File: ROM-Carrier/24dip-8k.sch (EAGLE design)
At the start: 7 parts

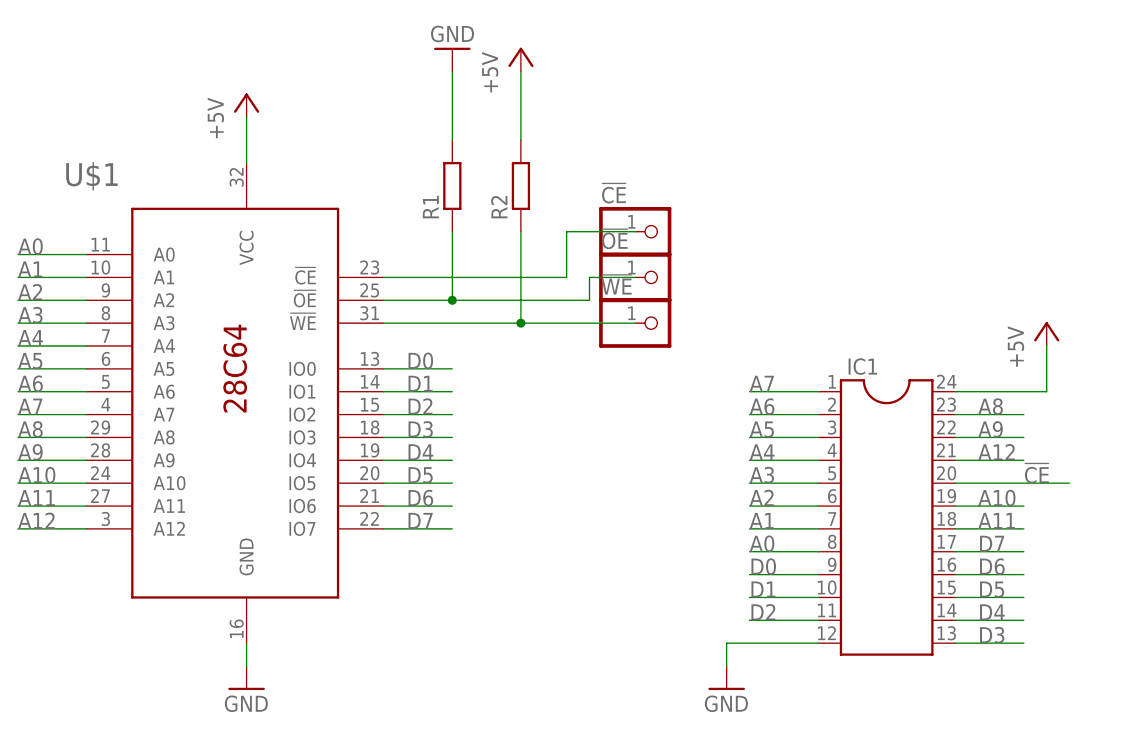
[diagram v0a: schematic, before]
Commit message: fix carrier board (was 24-9, needed to be 24-6) removed unnecessary z80 support from 8080 sim
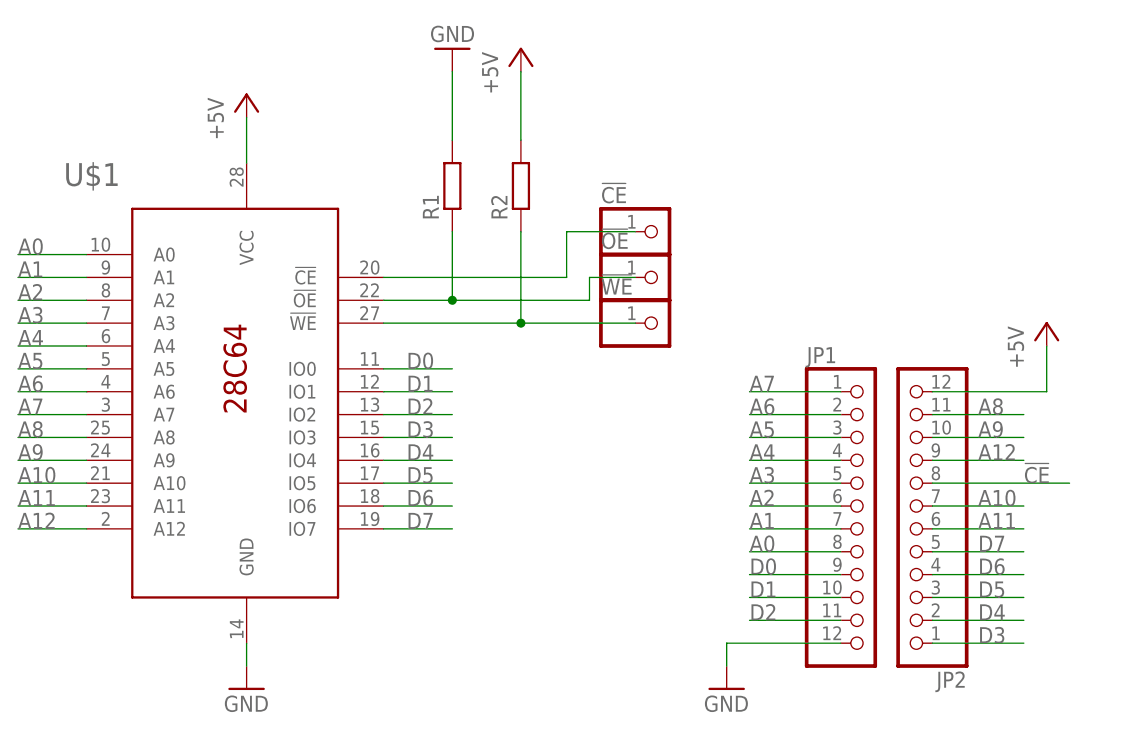
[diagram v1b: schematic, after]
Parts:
- removed IC1: (no value), ic-package:DIL24-9
- added JP1, JP2: (no value), pinhead:PINHD-1X12
- U$1: value AT28C64B32J -> AT28C64B28S; device eeprom:AT28C64B32J -> eeprom:AT28C64B28S
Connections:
- net !CE: now also JP2.8; no longer IC1.20
- net +5V: now also JP2.12; no longer IC1.24
- net A0: now also JP1.8; no longer IC1.8
- net A1: now also JP1.7; no longer IC1.7
- net A10: now also JP2.7; no longer IC1.19
- net A11: now also JP2.6; no longer IC1.18
- net A12: now also JP2.9; no longer IC1.21
- net A2: now also JP1.6; no longer IC1.6
- net A3: now also JP1.5; no longer IC1.5
- net A4: now also JP1.4; no longer IC1.4
- net A5: now also JP1.3; no longer IC1.3
- net A6: now also JP1.2; no longer IC1.2
- net A7: now also JP1.1; no longer IC1.1
- net A8: now also JP2.11; no longer IC1.23
- net A9: now also JP2.10; no longer IC1.22
- net D0: now also JP1.9; no longer IC1.9
- net D1: now also JP1.10; no longer IC1.10
- net D2: now also JP1.11; no longer IC1.11
- net D3: now also JP2.1; no longer IC1.13
- net D4: now also JP2.2; no longer IC1.14
- net D5: now also JP2.3; no longer IC1.15
- net D6: now also JP2.4; no longer IC1.16
- net D7: now also JP2.5; no longer IC1.17
- net GND: now also JP1.12; no longer IC1.12
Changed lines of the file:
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@@
 </classes>
 <parts>
-<part name="U$1" library="eeprom" deviceset="AT28C64B" device="32J"/>
-<part name="IC1" library="ic-package" deviceset="DIL24" device="-9"/>
+<part name="U$1" library="eeprom" deviceset="AT28C64B" device="28S" value="AT28C64B28S"/>
 <part name="R1" library="rcl" deviceset="R-EU_" device="R1206"/>
 <part name="R2" library="rcl" deviceset="R-EU_" device="R1206"/>
@@
 <part name="!OE" library="pinhead" deviceset="PINHD-1X1" device=""/>
 <part name="!WE" library="pinhead" deviceset="PINHD-1X1" device=""/>
+<part name="JP1" library="pinhead" deviceset="PINHD-1X12" device=""/>
+<part name="JP2" library="pinhead" deviceset="PINHD-1X12" device=""/>
 </parts>
 <sheets>
@@
 <instances>
 <instance part="U$1" gate="G$1" x="40.64" y="40.64"/>
-<instance part="IC1" gate="G$1" x="111.76" y="25.4"/>
 <instance part="R1" gate="G$1" x="63.5" y="63.5" rot="R90"/>
 <instance part="R2" gate="G$1" x="71.12" y="63.5" rot="R90"/>
@@
 <instance part="!OE" gate="G$1" x="86.36" y="53.34"/>
 <instance part="!WE" gate="G$1" x="86.36" y="48.26"/>
+<instance part="JP1" gate="G$1" x="109.22" y="27.94"/>
+<instance part="JP2" gate="G$1" x="114.3" y="25.4" rot="R180"/>
 </instances>
 <busses>
@@
 </segment>
 <segment>
-<pinref part="IC1" gate="G$1" pin="12"/>
-<wire x1="93.98" y1="12.7" x2="104.14" y2="12.7" width="0.1524" layer="91"/>
+<wire x1="93.98" y1="12.7" x2="106.68" y2="12.7" width="0.1524" layer="91"/>
 <pinref part="GND3" gate="1" pin="GND"/>
 <wire x1="93.98" y1="12.7" x2="93.98" y2="10.16" width="0.1524" layer="91"/>
+<pinref part="JP1" gate="G$1" pin="12"/>
 </segment>
 </net>
@@
 </segment>
 <segment>
-<pinref part="IC1" gate="G$1" pin="24"/>
-<wire x1="129.54" y1="40.64" x2="119.38" y2="40.64" width="0.1524" layer="91"/>
+<wire x1="129.54" y1="40.64" x2="116.84" y2="40.64" width="0.1524" layer="91"/>
 <pinref part="P+3" gate="1" pin="+5V"/>
 <wire x1="129.54" y1="40.64" x2="129.54" y2="45.72" width="0.1524" layer="91"/>
+<pinref part="JP2" gate="G$1" pin="12"/>
 </segment>
 </net>
@@
 </segment>
 <segment>
-<pinref part="IC1" gate="G$1" pin="8"/>
-<wire x1="96.52" y1="22.86" x2="104.14" y2="22.86" width="0.1524" layer="91"/>
+<wire x1="96.52" y1="22.86" x2="106.68" y2="22.86" width="0.1524" layer="91"/>
 <label x="96.52" y="22.86" size="1.778" layer="95"/>
+<pinref part="JP1" gate="G$1" pin="8"/>
 </segment>
 </net>
@@
 </segment>
 <segment>
-<pinref part="IC1" gate="G$1" pin="7"/>
-<wire x1="96.52" y1="25.4" x2="104.14" y2="25.4" width="0.1524" layer="91"/>
+<wire x1="96.52" y1="25.4" x2="106.68" y2="25.4" width="0.1524" layer="91"/>
 <label x="96.52" y="25.4" size="1.778" layer="95"/>
+<pinref part="JP1" gate="G$1" pin="7"/>
 </segment>
 </net>
@@
 </segment>
 <segment>
-<pinref part="IC1" gate="G$1" pin="6"/>
-<wire x1="96.52" y1="27.94" x2="104.14" y2="27.94" width="0.1524" layer="91"/>
+<wire x1="96.52" y1="27.94" x2="106.68" y2="27.94" width="0.1524" layer="91"/>
 <label x="96.52" y="27.94" size="1.778" layer="95"/>
+<pinref part="JP1" gate="G$1" pin="6"/>
 </segment>
 </net>
@@
 </segment>
 <segment>
-<pinref part="IC1" gate="G$1" pin="5"/>
-<wire x1="96.52" y1="30.48" x2="104.14" y2="30.48" width="0.1524" layer="91"/>
+<wire x1="96.52" y1="30.48" x2="106.68" y2="30.48" width="0.1524" layer="91"/>
 <label x="96.52" y="30.48" size="1.778" layer="95"/>
+<pinref part="JP1" gate="G$1" pin="5"/>
 </segment>
 </net>
@@
 </segment>
 <segment>
-<pinref part="IC1" gate="G$1" pin="4"/>
-<wire x1="96.52" y1="33.02" x2="104.14" y2="33.02" width="0.1524" layer="91"/>
+<wire x1="96.52" y1="33.02" x2="106.68" y2="33.02" width="0.1524" layer="91"/>
 <label x="96.52" y="33.02" size="1.778" layer="95"/>
+<pinref part="JP1" gate="G$1" pin="4"/>
 </segment>
 </net>
@@
 </segment>
 <segment>
-<pinref part="IC1" gate="G$1" pin="3"/>
-<wire x1="96.52" y1="35.56" x2="104.14" y2="35.56" width="0.1524" layer="91"/>
+<wire x1="96.52" y1="35.56" x2="106.68" y2="35.56" width="0.1524" layer="91"/>
 <label x="96.52" y="35.56" size="1.778" layer="95"/>
+<pinref part="JP1" gate="G$1" pin="3"/>
 </segment>
 </net>
@@
 </segment>
 <segment>
-<pinref part="IC1" gate="G$1" pin="2"/>
-<wire x1="96.52" y1="38.1" x2="104.14" y2="38.1" width="0.1524" layer="91"/>
+<wire x1="96.52" y1="38.1" x2="106.68" y2="38.1" width="0.1524" layer="91"/>
 <label x="96.52" y="38.1" size="1.778" layer="95"/>
+<pinref part="JP1" gate="G$1" pin="2"/>
 </segment>
 </net>
@@
 </segment>
 <segment>
-<pinref part="IC1" gate="G$1" pin="1"/>
-<wire x1="96.52" y1="40.64" x2="104.14" y2="40.64" width="0.1524" layer="91"/>
+<wire x1="96.52" y1="40.64" x2="106.68" y2="40.64" width="0.1524" layer="91"/>
 <label x="96.52" y="40.64" size="1.778" layer="95"/>
+<pinref part="JP1" gate="G$1" pin="1"/>
 </segment>
 </net>
@@
 </segment>
 <segment>
-<pinref part="IC1" gate="G$1" pin="23"/>
-<wire x1="127" y1="38.1" x2="119.38" y2="38.1" width="0.1524" layer="91"/>
+<wire x1="127" y1="38.1" x2="116.84" y2="38.1" width="0.1524" layer="91"/>
 <label x="121.92" y="38.1" size="1.778" layer="95"/>
+<pinref part="JP2" gate="G$1" pin="11"/>
 </segment>
 </net>
@@
 </segment>
 <segment>
-<pinref part="IC1" gate="G$1" pin="22"/>
-<wire x1="127" y1="35.56" x2="119.38" y2="35.56" width="0.1524" layer="91"/>
+<wire x1="127" y1="35.56" x2="116.84" y2="35.56" width="0.1524" layer="91"/>
 <label x="121.92" y="35.56" size="1.778" layer="95"/>
+<pinref part="JP2" gate="G$1" pin="10"/>
 </segment>
 </net>
@@
 </segment>
 <segment>
-<pinref part="IC1" gate="G$1" pin="19"/>
-<wire x1="127" y1="27.94" x2="119.38" y2="27.94" width="0.1524" layer="91"/>
+<wire x1="127" y1="27.94" x2="116.84" y2="27.94" width="0.1524" layer="91"/>
 <label x="121.92" y="27.94" size="1.778" layer="95"/>
+<pinref part="JP2" gate="G$1" pin="7"/>
 </segment>
 </net>
@@
 </segment>
 <segment>
-<pinref part="IC1" gate="G$1" pin="18"/>
-<wire x1="127" y1="25.4" x2="119.38" y2="25.4" width="0.1524" layer="91"/>
+<wire x1="127" y1="25.4" x2="116.84" y2="25.4" width="0.1524" layer="91"/>
 <label x="121.92" y="25.4" size="1.778" layer="95"/>
+<pinref part="JP2" gate="G$1" pin="6"/>
 </segment>
 </net>
@@
 </segment>
 <segment>
-<pinref part="IC1" gate="G$1" pin="21"/>
-<wire x1="127" y1="33.02" x2="119.38" y2="33.02" width="0.1524" layer="91"/>
+<wire x1="127" y1="33.02" x2="116.84" y2="33.02" width="0.1524" layer="91"/>
 <label x="121.92" y="33.02" size="1.778" layer="95"/>
+<pinref part="JP2" gate="G$1" pin="9"/>
 </segment>
 </net>
@@
 </segment>
 <segment>
-<pinref part="IC1" gate="G$1" pin="9"/>
-<wire x1="96.52" y1="20.32" x2="104.14" y2="20.32" width="0.1524" layer="91"/>
+<wire x1="96.52" y1="20.32" x2="106.68" y2="20.32" width="0.1524" layer="91"/>
 <label x="96.52" y="20.32" size="1.778" layer="95"/>
+<pinref part="JP1" gate="G$1" pin="9"/>
 </segment>
 </net>
@@
 </segment>
 <segment>
-<pinref part="IC1" gate="G$1" pin="10"/>
-<wire x1="96.52" y1="17.78" x2="104.14" y2="17.78" width="0.1524" layer="91"/>
+<wire x1="96.52" y1="17.78" x2="106.68" y2="17.78" width="0.1524" layer="91"/>
 <label x="96.52" y="17.78" size="1.778" layer="95"/>
+<pinref part="JP1" gate="G$1" pin="10"/>
 </segment>
 </net>
@@
 </segment>
 <segment>
-<pinref part="IC1" gate="G$1" pin="11"/>
-<wire x1="96.52" y1="15.24" x2="104.14" y2="15.24" width="0.1524" layer="91"/>
+<wire x1="96.52" y1="15.24" x2="106.68" y2="15.24" width="0.1524" layer="91"/>
 <label x="96.52" y="15.24" size="1.778" layer="95"/>
+<pinref part="JP1" gate="G$1" pin="11"/>
 </segment>
 </net>
@@
 </segment>
 <segment>
-<pinref part="IC1" gate="G$1" pin="13"/>
-<wire x1="127" y1="12.7" x2="119.38" y2="12.7" width="0.1524" layer="91"/>
+<wire x1="127" y1="12.7" x2="116.84" y2="12.7" width="0.1524" layer="91"/>
 <label x="121.92" y="12.7" size="1.778" layer="95"/>
+<pinref part="JP2" gate="G$1" pin="1"/>
 </segment>
 </net>
@@
 </segment>
 <segment>
-<pinref part="IC1" gate="G$1" pin="14"/>
-<wire x1="127" y1="15.24" x2="119.38" y2="15.24" width="0.1524" layer="91"/>
+<wire x1="127" y1="15.24" x2="116.84" y2="15.24" width="0.1524" layer="91"/>
 <label x="121.92" y="15.24" size="1.778" layer="95"/>
+<pinref part="JP2" gate="G$1" pin="2"/>
 </segment>
 </net>
@@
 </segment>
 <segment>
-<pinref part="IC1" gate="G$1" pin="15"/>
-<wire x1="127" y1="17.78" x2="119.38" y2="17.78" width="0.1524" layer="91"/>
+<wire x1="127" y1="17.78" x2="116.84" y2="17.78" width="0.1524" layer="91"/>
 <label x="121.92" y="17.78" size="1.778" layer="95"/>
+<pinref part="JP2" gate="G$1" pin="3"/>
 </segment>
 </net>
@@
 </segment>
 <segment>
-<pinref part="IC1" gate="G$1" pin="16"/>
-<wire x1="127" y1="20.32" x2="119.38" y2="20.32" width="0.1524" layer="91"/>
+<wire x1="127" y1="20.32" x2="116.84" y2="20.32" width="0.1524" layer="91"/>
 <label x="121.92" y="20.32" size="1.778" layer="95"/>
+<pinref part="JP2" gate="G$1" pin="4"/>
 </segment>
 </net>
@@
 </segment>
 <segment>
-<pinref part="IC1" gate="G$1" pin="17"/>
-<wire x1="127" y1="22.86" x2="119.38" y2="22.86" width="0.1524" layer="91"/>
+<wire x1="127" y1="22.86" x2="116.84" y2="22.86" width="0.1524" layer="91"/>
 <label x="121.92" y="22.86" size="1.778" layer="95"/>
+<pinref part="JP2" gate="G$1" pin="5"/>
 </segment>
 </net>
 <net name="!CE" class="0">
 <segment>
-<pinref part="IC1" gate="G$1" pin="20"/>
-<wire x1="132.08" y1="30.48" x2="119.38" y2="30.48" width="0.1524" layer="91"/>
+<wire x1="132.08" y1="30.48" x2="116.84" y2="30.48" width="0.1524" layer="91"/>
 <label x="127" y="30.48" size="1.778" layer="95"/>
-</segment>
-<segment>
+<pinref part="JP2" gate="G$1" pin="8"/>
+</segment>
+<segment>
